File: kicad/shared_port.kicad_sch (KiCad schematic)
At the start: 28 parts, among them J1 Keyboard, J2 SNES pad, J3 SNES pad, J4 SD (SPI), J5 PS/2 mouse, U37 SN74HC574N, U38 ATF22V10C-7PX, U39 SN74F541N

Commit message: Tidy every schematic sheet: spread parts, straight runs, buses kept, horizontal tabs
Shared port, expansion and cartridge sheets laid out by hand; buses from
other sheets get a bus label at each chip, busy control nets a label at
each pin; some PLD and connector symbols reordered so wires run straight;
sideways power symbols read across. 0 netlist problems, no overlaps.

Co-Authored-By: Claude Opus 5.5 (1M context) <noreply@anthropic.com>
Claude-Session: https://claude.ai/code/session_01L9AkLuEg13EebxDmgXsaEp
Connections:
- net P_PS2D: now reaches D1003.1 (K), U37.16 (Q3)
- net P_CS: now reaches D1002.1 (K), R1005.1, U37.17 (Q2)
- net P_MOSI: now reaches J2.3 (LATCH), J3.3 (LATCH), R1004.1, U37.18 (Q1)
- net P_SCK: now reaches J2.2 (CLOCK), J3.2 (CLOCK), R1003.1, U37.19 (Q0)
- net PAD2_DATA: now reaches J3.4 (DATA), R1002.2, U38.8 (PAD2)
- net PAD1_DATA: now reaches J2.4 (DATA), R1001.2, U38.7 (PAD1)
- net K0: no longer names the net of U37.15 (Q4), U38.3 (K0)
- net K1: no longer names the net of U37.14 (Q5), U38.4 (K1)
- net K2: no longer names the net of U37.13 (Q6), U38.5 (K2)
- net K3: no longer names the net of U37.12 (Q7), U38.6 (K3)
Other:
- moved on the sheet: C37, C38, U37, U38

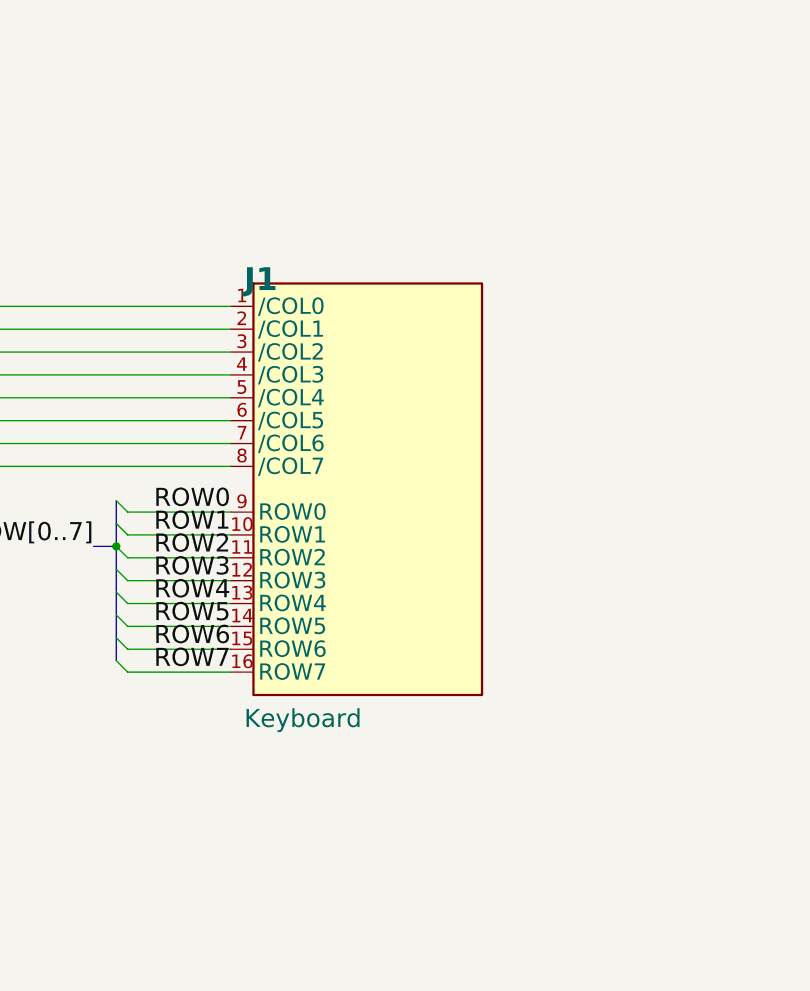
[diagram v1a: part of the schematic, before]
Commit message: Keyboard board schematic and Cherry MX LED footprints; J1 keyed 2x10 box header
- gen_kicad_keyswitch.py writes placard:SW_Cherry_MX_LED_<size>u_PCB (1u-6.25u):
  stock MX PCB-mount pads and stabilizer holes plus 3 mm LED pads
- kicad/keyboard/: 63 keys (SW_Push_LED), BAT85 per key, always-on LED with 1k
- Keyboard_Header: 2x10 shrouded box header, 17 +5V, 18-19 GND, 20 spare;
  main-board J1 updated
- schematics/placard_keyboard.pdf; IO.md and kicad/README.md updated

Co-Authored-By: Claude Opus 5.5 (1M context) <noreply@anthropic.com>
Claude-Session: https://claude.ai/code/session_01RmACANBz9vH4tGXSeZdY5H
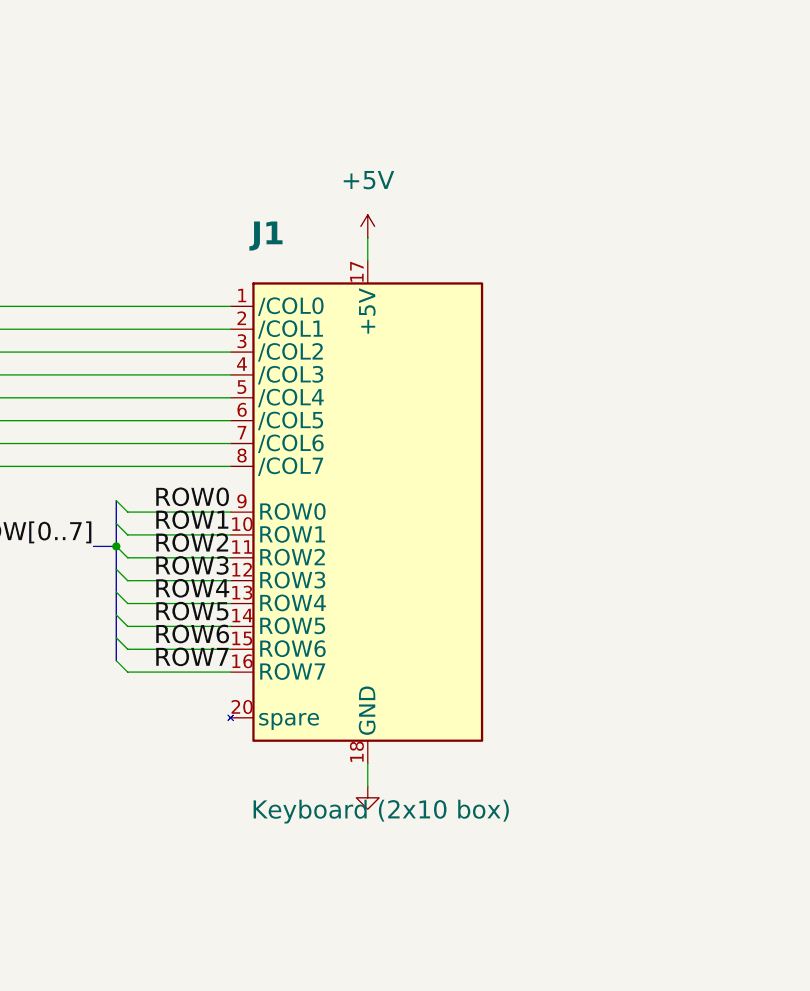
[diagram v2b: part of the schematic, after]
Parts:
- J1: value Keyboard -> Keyboard (2x10 box); footprint Connector_PinHeader_2.54mm:PinHeader_1x16_P2.54mm_Vertical -> Connector_IDC:IDC-Header_2x10_P2.54mm_Vertical
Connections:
- net +5V: now also J1.17 (+5V)
- net GND: now also J1.18 (GND), J1.19 (GND)

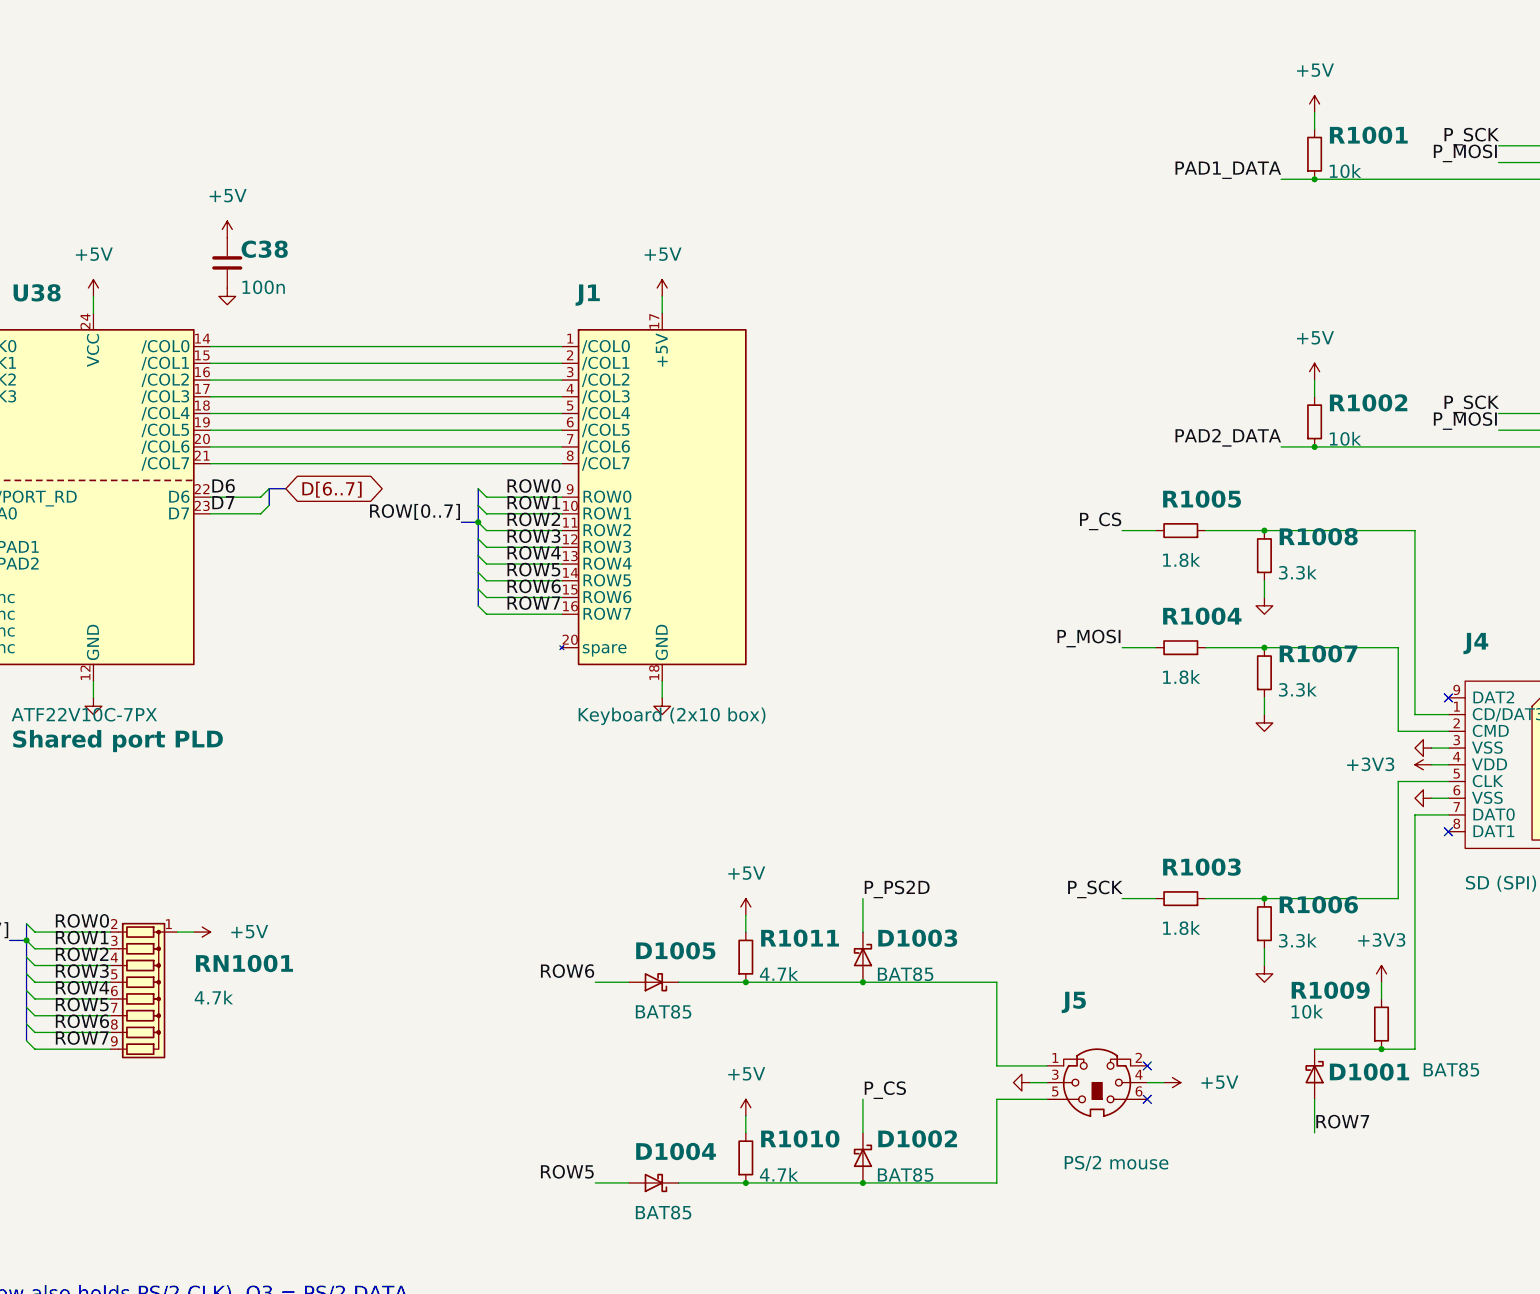
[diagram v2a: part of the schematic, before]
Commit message: Number parts from 1 for each kind; US zigzag resistor symbols
Main board R1-R54, RN1-RN2, D1-D5, JP1-JP2, F1, NT1, non-decoupling
capacitors C41-C46 (decaps keep Cn = Un); keyboard keys 1-63 row by row
(SWn, Dn, Rn per key). Resistors use R_US / R_Network08_US. --check now
fails on gaps or hundreds in the numbering. PDFs regenerated.

Co-Authored-By: Claude Opus 5.5 (1M context) <noreply@anthropic.com>
Claude-Session: https://claude.ai/code/session_01L9AkLuEg13EebxDmgXsaEp
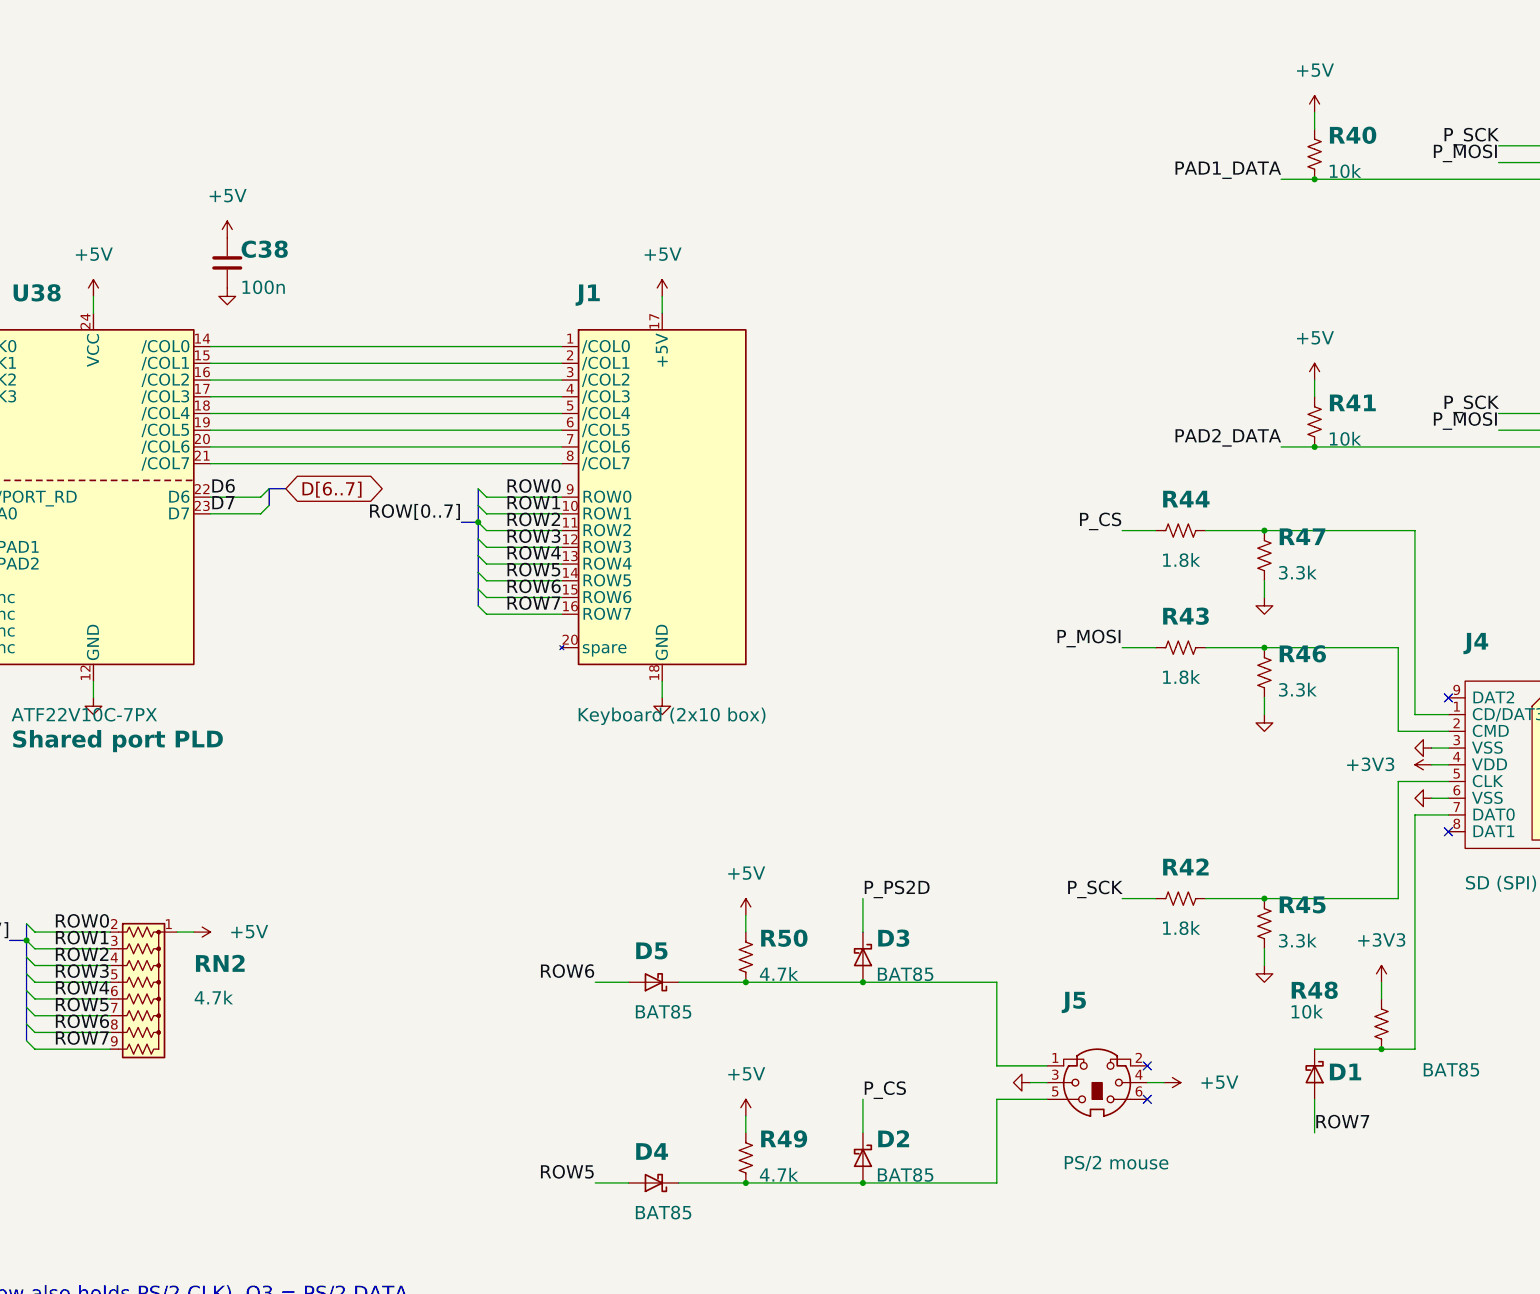
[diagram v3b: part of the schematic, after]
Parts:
- removed D1001, D1002, D1003, D1004, D1005: BAT85, Diode_THT:D_DO-35_SOD27_P7.62mm_Horizontal, symbol placard_std:D_Schottky
- removed R1001, R1002, R1009: 10k, Resistor_THT:R_Axial_DIN0207_L6.3mm_D2.5mm_P10.16mm_Horizontal, symbol placard_std:R
- removed R1003, R1004, R1005: 1.8k, Resistor_THT:R_Axial_DIN0207_L6.3mm_D2.5mm_P10.16mm_Horizontal, symbol placard_std:R
- removed R1006, R1007, R1008: 3.3k, Resistor_THT:R_Axial_DIN0207_L6.3mm_D2.5mm_P10.16mm_Horizontal, symbol placard_std:R
- removed R1010, R1011: 4.7k, Resistor_THT:R_Axial_DIN0207_L6.3mm_D2.5mm_P10.16mm_Horizontal, symbol placard_std:R
- removed RN1001: 4.7k, Resistor_THT:R_Array_SIP9, symbol placard_std:R_Network08
- added D1, D2, D3, D4, D5: BAT85, Diode_THT:D_DO-35_SOD27_P7.62mm_Horizontal, symbol placard_std:D_Schottky
- added R40, R41, R48: 10k, Resistor_THT:R_Axial_DIN0207_L6.3mm_D2.5mm_P10.16mm_Horizontal, symbol placard_std:R_US
- added R42, R43, R44: 1.8k, Resistor_THT:R_Axial_DIN0207_L6.3mm_D2.5mm_P10.16mm_Horizontal, symbol placard_std:R_US
- added R45, R46, R47: 3.3k, Resistor_THT:R_Axial_DIN0207_L6.3mm_D2.5mm_P10.16mm_Horizontal, symbol placard_std:R_US
- added R49, R50: 4.7k, Resistor_THT:R_Axial_DIN0207_L6.3mm_D2.5mm_P10.16mm_Horizontal, symbol placard_std:R_US
- added RN2: 4.7k, Resistor_THT:R_Array_SIP9, symbol placard_std:R_Network08_US
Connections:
- net +3V3: now also R48.1
- net +5V: now also R40.1, R41.1, R49.1, R50.1, RN2.1 (common)
- net GND: now also R45.2, R46.2, R47.2
- net PAD1_DATA: now also R40.2
- net PAD2_DATA: now also R41.2
- net P_CS: now also D2.1 (K), R44.1
- net P_MOSI: now also R43.1
- net P_PS2D: now also D3.1 (K)
- net P_SCK: now also R42.1
- net ROW0: now also RN2.2 (R1)
- net ROW1: now also RN2.3 (R2)
- net ROW2: now also RN2.4 (R3)
- net ROW3: now also RN2.5 (R4)
- net ROW4: now also RN2.6 (R5)
- net ROW5: now also D4.2 (A), RN2.7 (R6)
- net ROW6: now also D5.2 (A), RN2.8 (R7)
- net ROW7: now also D1.2 (A), RN2.9 (R8)
- net at J5.1: now also D3.2 (A), D5.1 (K), R50.2
- net at J4.2 (CMD): now also R43.2, R46.1
- net at J4.1 (CD/DAT3): now also R44.2, R47.1
- net at J5.5: now also D2.2 (A), D4.1 (K), R49.2
- net at J4.5 (CLK): now also R42.2, R45.1
- net at J4.7 (DAT0): now also D1.1 (K), R48.2

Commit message: Bill of materials for the main board, cartridge and keyboard
Manufacturer and MPN fields on every schematic part (empty where none is
chosen), set from an MPN table in gen_kicad_schematic.py; net tie, cartridge
edge fingers and solder jumper excluded from the BOM.  gen_bom.py groups the
parts by part number into docs/BOM.md and docs/BOM.csv, adding sockets,
shunts, keyboard LEDs, keycaps, stabilizers and the keyboard ribbon cable.

Co-Authored-By: Claude Opus 5.5 (1M context) <noreply@anthropic.com>
Claude-Session: https://claude.ai/code/session_018iEnPngycbxX6Tt4Wzp3zN
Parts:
- D1, D2, D3, D4, D5: MPN (none) -> BAT85; Manufacturer (none) -> Vishay
- U37: MPN (none) -> SN74HC574N; Manufacturer (none) -> Texas Instruments
- U38: MPN (none) -> ATF22V10C-7PX; Manufacturer (none) -> Microchip
- U39: MPN (none) -> SN74F541N; Manufacturer (none) -> Texas Instruments
